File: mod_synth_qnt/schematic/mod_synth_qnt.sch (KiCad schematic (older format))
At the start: 22 parts

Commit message: Update schematic and code
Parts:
- added D? (x3): 1N4148, Diode_THT:D_DO-35_SOD27_P7.62mm_Horizontal, symbol Diode:1N4148
- added J?: Gate, symbol Connector:AudioJack2
- added R? (x3): 10k, symbol Device:R
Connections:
- net GND: now also J?.S, R?.1, R?.1, R?.2
- net IN_1: now also D?.1 (K); no longer C?.1, J?.T
- net IN_2: now also D?.1 (K); no longer C?.1, J?.T
- new net: C?.1, D?.2 (A), J?.T, R?.2 (x2)
- new net: D?.2 (A), J?.T, R?.1
- new net IN_GATE: D?.1 (K)
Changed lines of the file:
@@
 	-1   0    0    -1
 $EndComp
-Text Label 3200 2300 0    50   ~ 0
+Text Label 4300 2300 0    50   ~ 0
 IN_1
-Text Label 3200 3100 0    50   ~ 0
+Text Label 4300 3100 0    50   ~ 0
 IN_2
 $Comp
@@
 Wire Wire Line
 	3200 2950 3200 3000
-Wire Wire Line
-	3200 3100 3075 3100
-Wire Wire Line
-	3200 2300 3075 2300
 Text Label 6225 2925 0    50   ~ 0
 IN_1
@@
 L power:GND #PWR?
 U 1 1 5D619ACB
-P 3075 2600
-F 0 "#PWR?" H 3075 2350 50  0001 C CNN
-F 1 "GND" H 3080 2427 50  0000 C CNN
-F 2 "" H 3075 2600 50  0001 C CNN
-F 3 "" H 3075 2600 50  0001 C CNN
-	1    3075 2600
+P 3075 2675
+F 0 "#PWR?" H 3075 2425 50  0001 C CNN
+F 1 "GND" H 3080 2502 50  0000 C CNN
+F 2 "" H 3075 2675 50  0001 C CNN
+F 3 "" H 3075 2675 50  0001 C CNN
+	1    3075 2675
 	1    0    0    -1
 $EndComp
@@
 L power:GND #PWR?
 U 1 1 5D61A0C8
-P 3075 3375
-F 0 "#PWR?" H 3075 3125 50  0001 C CNN
-F 1 "GND" H 3080 3202 50  0000 C CNN
-F 2 "" H 3075 3375 50  0001 C CNN
-F 3 "" H 3075 3375 50  0001 C CNN
-	1    3075 3375
+P 3075 3450
+F 0 "#PWR?" H 3075 3200 50  0001 C CNN
+F 1 "GND" H 3080 3277 50  0000 C CNN
+F 2 "" H 3075 3450 50  0001 C CNN
+F 3 "" H 3075 3450 50  0001 C CNN
+	1    3075 3450
 	1    0    0    -1
 $EndComp
 Wire Wire Line
 	3075 2600 3075 2500
-Wire Wire Line
-	3075 3300 3075 3375
 $Comp
 L power:GND #PWR?
@@
 NoConn ~ 8275 5300
 NoConn ~ 8275 5200
+$Comp
+L Device:R R?
+U 1 1 5D61316C
+P 3550 2450
+F 0 "R?" V 3343 2450 50  0000 C CNN
+F 1 "10k" V 3434 2450 50  0000 C CNN
+F 2 "" V 3480 2450 50  0001 C CNN
+F 3 "~" H 3550 2450 50  0001 C CNN
+	1    3550 2450
+	-1   0    0    1
+$EndComp
+$Comp
+L Device:R R?
+U 1 1 5D6143B5
+P 3550 3250
+F 0 "R?" V 3343 3250 50  0000 C CNN
+F 1 "10k" V 3434 3250 50  0000 C CNN
+F 2 "" V 3480 3250 50  0001 C CNN
+F 3 "~" H 3550 3250 50  0001 C CNN
+	1    3550 3250
+	-1   0    0    1
+$EndComp
+Wire Wire Line
+	3075 2300 3550 2300
+Wire Wire Line
+	3550 2300 3800 2300
+Connection ~ 3550 2300
+Wire Wire Line
+	3075 3100 3550 3100
+Connection ~ 3550 3100
+Wire Wire Line
+	3550 3100 3800 3100
+Wire Wire Line
+	3550 2600 3075 2600
+Wire Wire Line
+	3075 2600 3075 2675
+Connection ~ 3075 2600
+Wire Wire Line
+	3550 3400 3075 3400
+Wire Wire Line
+	3075 3300 3075 3400
+Connection ~ 3075 3400
+Wire Wire Line
+	3075 3400 3075 3450
+$Comp
+L Connector:AudioJack2 J?
+U 1 1 5D62A188
+P 2800 1650
+F 0 "J?" H 2832 1975 50  0000 C CNN
+F 1 "Gate" H 2832 1884 50  0000 C CNN
+F 2 "" H 2800 1650 50  0001 C CNN
+F 3 "~" H 2800 1650 50  0001 C CNN
+	1    2800 1650
+	1    0    0    -1
+$EndComp
+$Comp
+L power:GND #PWR?
+U 1 1 5D62A425
+P 3200 1225
+F 0 "#PWR?" H 3200 975 50  0001 C CNN
+F 1 "GND" H 3205 1052 50  0000 C CNN
+F 2 "" H 3200 1225 50  0001 C CNN
+F 3 "" H 3200 1225 50  0001 C CNN
+	1    3200 1225
+	-1   0    0    1
+$EndComp
+Wire Wire Line
+	3000 1550 3200 1550
+Text Label 4300 1650 0    50   ~ 0
+IN_GATE
+Wire Wire Line
+	3000 1650 3550 1650
+$Comp
+L Diode:1N4148 D?
+U 1 1 5D630B6B
+P 3925 1650
+F 0 "D?" H 3925 1434 50  0000 C CNN
+F 1 "1N4148" H 3925 1525 50  0000 C CNN
+F 2 "Diode_THT:D_DO-35_SOD27_P7.62mm_Horizontal" H 3925 1475 50  0001 C CNN
+F 3 "https://assets.nexperia.com/documents/data-sheet/1N4148_1N4448.pdf" H 3925 1650 50  0001 C CNN
+	1    3925 1650
+	-1   0    0    1
+$EndComp
+$Comp
+L Diode:1N4148 D?
+U 1 1 5D631B5D
+P 3950 2300
+F 0 "D?" H 3950 2084 50  0000 C CNN
+F 1 "1N4148" H 3950 2175 50  0000 C CNN
+F 2 "Diode_THT:D_DO-35_SOD27_P7.62mm_Horizontal" H 3950 2125 50  0001 C CNN
+F 3 "https://assets.nexperia.com/documents/data-sheet/1N4148_1N4448.pdf" H 3950 2300 50  0001 C CNN
+	1    3950 2300
+	-1   0    0    1
+$EndComp
+$Comp
+L Diode:1N4148 D?
+U 1 1 5D631FDA
+P 3950 3100
+F 0 "D?" H 3950 2884 50  0000 C CNN
+F 1 "1N4148" H 3950 2975 50  0000 C CNN
+F 2 "Diode_THT:D_DO-35_SOD27_P7.62mm_Horizontal" H 3950 2925 50  0001 C CNN
+F 3 "https://assets.nexperia.com/documents/data-sheet/1N4148_1N4448.pdf" H 3950 3100 50  0001 C CNN
+	1    3950 3100
+	-1   0    0    1
+$EndComp
+$Comp
+L Device:R R?
+U 1 1 5D633789
+P 3550 1500
+F 0 "R?" V 3343 1500 50  0000 C CNN
+F 1 "10k" V 3434 1500 50  0000 C CNN
+F 2 "" V 3480 1500 50  0001 C CNN
+F 3 "~" H 3550 1500 50  0001 C CNN
+	1    3550 1500
+	-1   0    0    1
+$EndComp
+Connection ~ 3550 1650
+Wire Wire Line
+	3550 1650 3775 1650
+Wire Wire Line
+	4075 1650 4300 1650
+Wire Wire Line
+	4300 2300 4100 2300
+Wire Wire Line
+	4100 3100 4300 3100
+Wire Wire Line
+	3200 1225 3200 1350
+Wire Wire Line
+	3550 1350 3200 1350
+Connection ~ 3200 1350
+Wire Wire Line
+	3200 1350 3200 1550
 $EndSCHEMATC

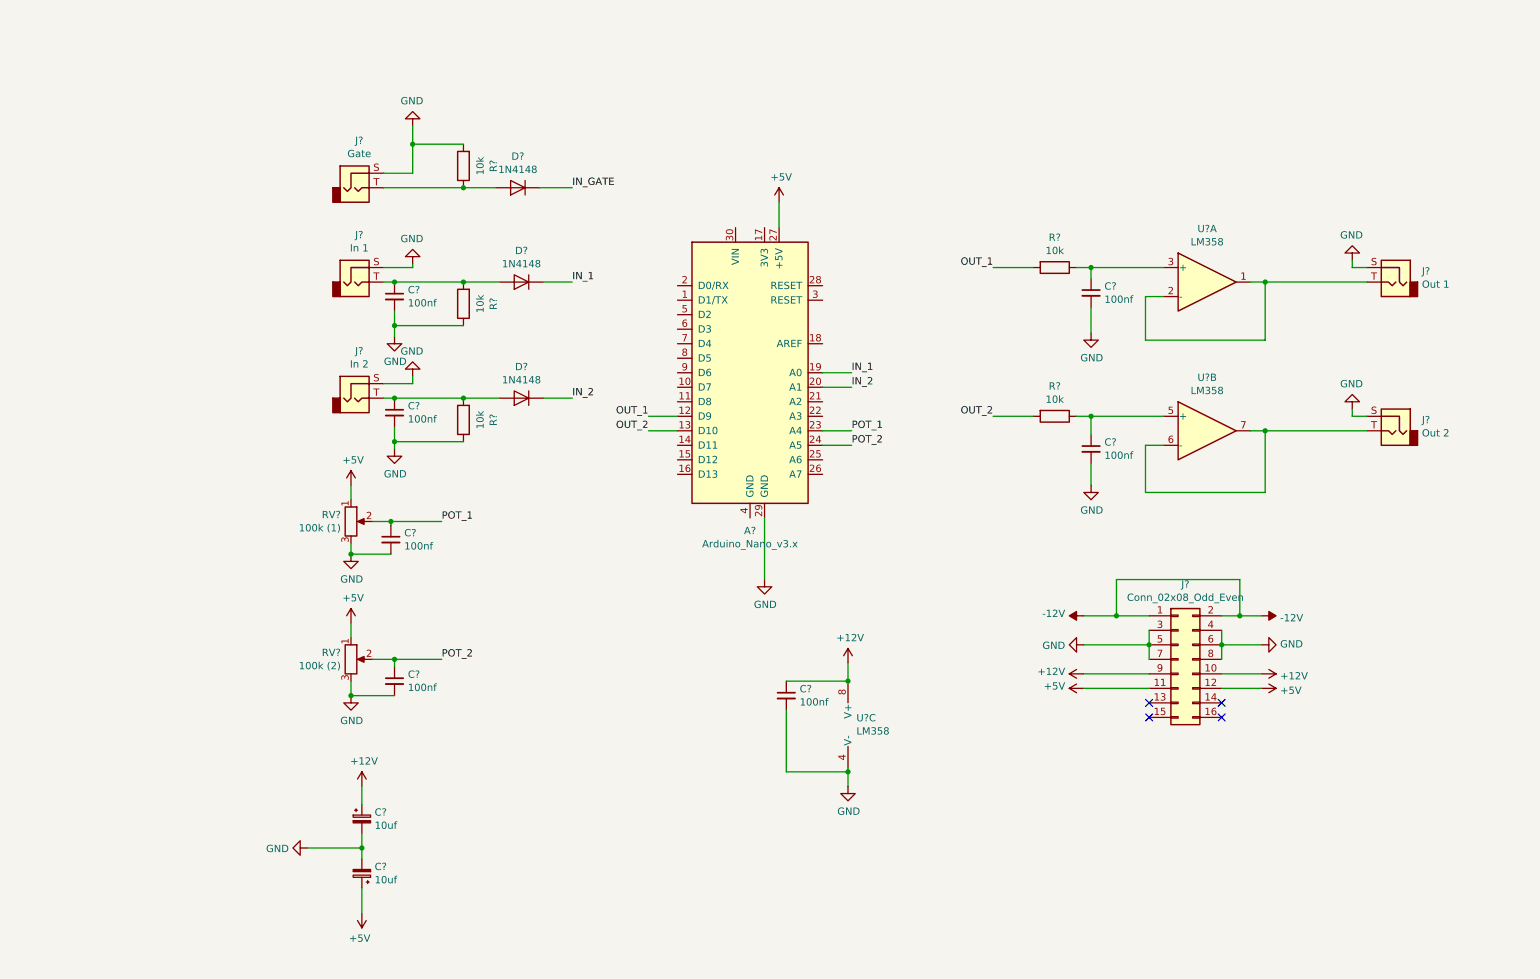
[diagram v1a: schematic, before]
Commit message: Add scale/note input and led output
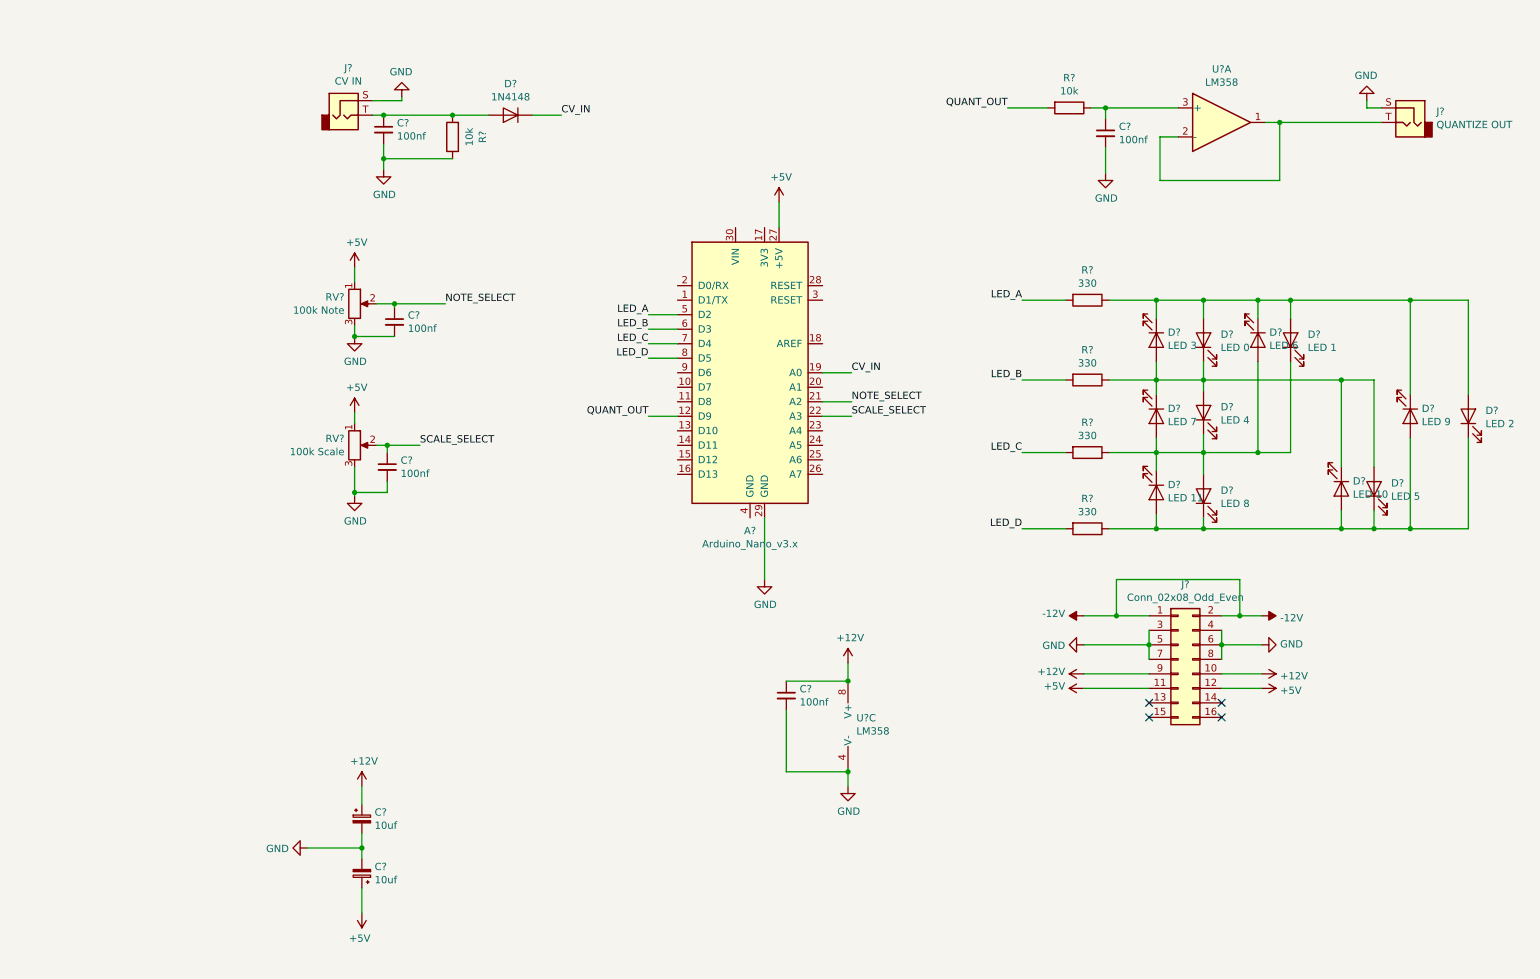
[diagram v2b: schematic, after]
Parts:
- removed C? (x3): 100nf, symbol Device:C_Small
- removed D? (x2): 1N4148, Diode_THT:D_DO-35_SOD27_P7.62mm_Horizontal, symbol Diode:1N4148
- removed J?: Out 2, symbol Connector:AudioJack2
- removed J?: In 2, symbol Connector:AudioJack2
- removed J?: Gate, symbol Connector:AudioJack2
- removed R? (x3): 10k, symbol Device:R
- removed RV?: 100k (2), symbol Device:R_POT
- removed U?: LM358, symbol Amplifier_Operational:LM358
- added C?: 100nf, symbol Device:C_Small
- added D?: LED 3, symbol Device:LED
- added D?: LED 7, symbol Device:LED
- added D?: LED 11, symbol Device:LED
- added D?: LED 6, symbol Device:LED
- added D?: LED 10, symbol Device:LED
- added D?: LED 9, symbol Device:LED
- added D?: LED 2, symbol Device:LED
- added D?: LED 0, symbol Device:LED
- added D?: LED 4, symbol Device:LED
- added D?: LED 8, symbol Device:LED
- added D?: LED 1, symbol Device:LED
- added D?: LED 5, symbol Device:LED
- added R? (x4): 330, symbol Device:R
- added RV?: 100k Scale, symbol Device:R_POT
- J?: value In 1 -> CV IN
- J?: value Out 1 -> QUANTIZE OUT
- RV?: value 100k (1) -> 100k Note
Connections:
- net +5V: now also RV?.1
- net GND: now also C?.2, RV?.3
- net NOTE_SELECT: now reaches A?.21 (A2)
- net NOTE_SELECT: now also C?.1, RV?.2
- net SCALE_SELECT: now reaches A?.22 (A3)
- net SCALE_SELECT: now also C?.1, RV?.2
- net LED_A: now reaches A?.5 (D2)
- net LED_A: now also R?.2
- net LED_B: now reaches A?.6 (D3)
- net LED_B: now also R?.2
- net LED_C: now reaches A?.7 (D4)
- net LED_C: now also R?.2
- net LED_D: now reaches A?.8 (D5)
- net LED_D: now also R?.2
- net IN_1 renamed CV_IN
- net IN_2: no longer names the net of A?.20 (A1)
- net OUT_1 renamed QUANT_OUT
- net OUT_2: no longer names the net of A?.13 (D10)
- removed net POT_1: A?.23 (A4), C?.1, RV?.2
- net POT_2: no longer names the net of A?.24 (A5)
- new net: D?.1 (K), D?.1 (K), D?.1 (K), D?.2 (A), D?.2 (A), D?.2 (A), R?.1 (x4)
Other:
- moved on the sheet: C?, D?, J?, R?, RV?, U?A

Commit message: Improve code, start PCB layout
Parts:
- added J4, J7: Conn_01x07_Male, Connector_PinHeader_2.54mm:PinHeader_1x07_P2.54mm_Vertical, symbol Connector:Conn_01x07_Male
- added J5, J6: Conn_01x07_Female, Connector_PinSocket_2.54mm:PinSocket_1x07_P2.54mm_Vertical, symbol Connector:Conn_01x07_Female
- C1, C2: renamed from C?; footprint (none) -> Capacitor_THT:CP_Radial_D5.0mm_P2.00mm
- C3, C4, C5, C6, C7: renamed from C?; footprint (none) -> Capacitor_THT:C_Disc_D9.0mm_W2.5mm_P5.00mm
- D10, D11, D12, D13, D2, D3, D4, D5, D6, D7, D8, D9: renamed from D?; footprint (none) -> LED_THT:LED_D5.0mm
- J1, J3: renamed from J?; footprint (none) -> Connector_Audio:Jack_3.5mm_QingPu_WQP-PJ398SM_Vertical_CircularHoles
- J2: renamed from J?; footprint (none) -> Connector_IDC:IDC-Header_2x08_P2.54mm_Vertical
- R1, R2, R3, R4, R5, R6: renamed from R?; footprint (none) -> Resistor_THT:R_Axial_DIN0207_L6.3mm_D2.5mm_P10.16mm_Horizontal
- RV1, RV2: renamed from RV?; footprint (none) -> Potentiometer_THT:Potentiometer_Alpha_RD901F-40-00D_Single_Vertical
- U1: renamed from U?; footprint (none) -> Package_DIP:DIP-8_W7.62mm_Socket_LongPads
- gave numbers to parts that had none: 3
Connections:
- net GND: now also J5.1 (Pin_1); no longer C3.2, C4.2, C5.2, J1.S, J3.S, RV1.3, RV2.3
- net CV_IN_PCB_A: now reaches D1.2 (A), R1.2
- net CV_IN_PCB_A: now also J5.6 (Pin_6); no longer C3.1, J1.T
- net Q_OUT_PCB_A: now reaches U1.1, U1.2 (-)
- net Q_OUT_PCB_A: now also J5.7 (Pin_7); no longer J3.T
- new net CV_IN_PCB_B: C3.1, J1.T, J4.6 (Pin_6)
- new net GND_PCB_B: C3.2, C4.2, C5.2, J1.S, J3.S, J4.1 (Pin_1), RV1.3, RV2.3
- new net Q_OUT_PCB_B: J3.T, J4.7 (Pin_7)
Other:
- moved on the sheet: A1, C1, C2, C3, C4, C5, C6, D1, J1, J2, R1, RV1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

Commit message: finish layout
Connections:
- net +5V: now also J5.5 (Pin_5); no longer RV1.1, RV2.1
- net LED_A: now also J6.2 (Pin_2), R3.1; no longer A1.5 (D2), R3.2
- net LED_B: now also J6.3 (Pin_3), R4.1; no longer A1.6 (D3), R4.2
- net LED_C: now also J6.4 (Pin_4), R5.1; no longer A1.7 (D4), R5.2
- net LED_D: now also J6.5 (Pin_5), R6.1; no longer A1.8 (D5), R6.2
- net NOTE_SELECT: now also J6.7 (Pin_7); no longer C5.1, RV1.2
- net SCALE_SELECT: now also J6.6 (Pin_6); no longer C4.1, RV2.2
- net LED_A_PCB_B: now reaches D12.1 (K), D13.2 (A), D2.1 (K), D5.2 (A), D8.1 (K), D9.2 (A)
- net LED_A_PCB_B: now also J7.2 (Pin_2); no longer R3.1
- net LED_B_PCB_B: now reaches D10.1 (K), D11.2 (A), D2.2 (A), D3.1 (K), D5.1 (K), D6.2 (A)
- net LED_B_PCB_B: now also J7.3 (Pin_3); no longer R4.1
- net LED_C_PCB_B: now reaches D3.2 (A), D4.1 (K), D6.1 (K), D7.2 (A), D8.2 (A), D9.1 (K)
- net LED_C_PCB_B: now also J7.4 (Pin_4); no longer R5.1
- net LED_D_PCB_B: now reaches D10.2 (A), D11.1 (K), D12.2 (A), D13.1 (K), D4.2 (A), D7.1 (K)
- net LED_D_PCB_B: now also J7.5 (Pin_5); no longer R6.1
- net 5V_PCB_B: now reaches J4.5 (Pin_5)
- net 5V_PCB_B: now also RV1.1, RV2.1
- net SCALE_SELECT_PCB_B: now reaches J7.6 (Pin_6)
- net SCALE_SELECT_PCB_B: now also C4.1, RV2.2
- net NOTE_SELECT_PCB_B: now reaches J7.7 (Pin_7)
- net NOTE_SELECT_PCB_B: now also C5.1, RV1.2
- new net: A1.5 (D2), R3.2
- new net: A1.6 (D3), R4.2
- new net: A1.7 (D4), R5.2
- new net: A1.8 (D5), R6.2
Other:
- moved on the sheet: R3, R4, R5, R6
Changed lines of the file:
@@
 Wire Wire Line
 	1300 2825 1025 2825
-$Comp
-L power:+5V #PWR0116
-U 1 1 5D6276B5
-P 1025 2350
-F 0 "#PWR0116" H 1025 2200 50  0001 C CNN
-F 1 "+5V" H 1040 2523 50  0000 C CNN
-F 2 "" H 1025 2350 50  0001 C CNN
-F 3 "" H 1025 2350 50  0001 C CNN
-	1    1025 2350
-	1    0    0    -1
-$EndComp
 Wire Wire Line
 	1025 2350 1025 2450
 Text Label 1650 2600 0    50   ~ 0
-NOTE_SELECT
+NOTE_SELECT_PCB_B
 Wire Wire Line
 	1650 2600 1300 2600
@@
 Wire Wire Line
 	3125 1000 2925 1000
-Text Label 3950 1700 2    50   ~ 0
+Text Label 3350 1700 2    50   ~ 0
 LED_A
-Text Label 3950 1800 2    50   ~ 0
+Text Label 3350 1800 2    50   ~ 0
 LED_B
-Text Label 3950 1900 2    50   ~ 0
+Text Label 3350 1900 2    50   ~ 0
 LED_C
-Text Label 3950 2000 2    50   ~ 0
+Text Label 3350 2000 2    50   ~ 0
 LED_D
 Wire Wire Line
-	3950 1700 4150 1700
-Wire Wire Line
-	4150 1800 3950 1800
-Wire Wire Line
-	3950 1900 4150 1900
-Wire Wire Line
-	4150 2000 3950 2000
+	3350 1700 3550 1700
+Wire Wire Line
+	3550 1800 3350 1800
+Wire Wire Line
+	3350 1900 3550 1900
+Wire Wire Line
+	3550 2000 3350 2000
 Text Label 5350 2300 0    50   ~ 0
 NOTE_SELECT
@@
 $EndComp
 $Comp
-L power:+5V #PWR0122
-U 1 1 5D643E11
-P 1000 3625
-F 0 "#PWR0122" H 1000 3475 50  0001 C CNN
-F 1 "+5V" H 1015 3798 50  0000 C CNN
-F 2 "" H 1000 3625 50  0001 C CNN
-F 3 "" H 1000 3625 50  0001 C CNN
-	1    1000 3625
-	1    0    0    -1
-$EndComp
-$Comp
 L Device:C_Small C4
 U 1 1 5D644560
@@
 	1225 4175 1000 4175
 Text Label 1450 3850 0    50   ~ 0
-SCALE_SELECT
+SCALE_SELECT_PCB_B
 Wire Wire Line
 	1150 3850 1225 3850
@@
 L Device:R R3
 U 1 1 5D64DAFD
-P 7850 2425
-F 0 "R3" V 7643 2425 50  0000 C CNN
-F 1 "330" V 7734 2425 50  0000 C CNN
-F 2 "Resistor_THT:R_Axial_DIN0207_L6.3mm_D2.5mm_P10.16mm_Horizontal" V 7780 2425 50  0001 C CNN
-F 3 "~" H 7850 2425 50  0001 C CNN
-	1    7850 2425
-	0    1    1    0
+P 3700 1700
+F 0 "R3" V 3493 1700 50  0000 C CNN
+F 1 "330" V 3584 1700 50  0000 C CNN
+F 2 "Resistor_THT:R_Axial_DIN0207_L6.3mm_D2.5mm_P10.16mm_Horizontal" V 3630 1700 50  0001 C CNN
+F 3 "~" H 3700 1700 50  0001 C CNN
+	1    3700 1700
+	0    -1   -1   0
 $EndComp
 $Comp
 L Device:R R4
 U 1 1 5D64E557
-P 7850 2975
-F 0 "R4" V 7643 2975 50  0000 C CNN
-F 1 "330" V 7734 2975 50  0000 C CNN
-F 2 "Resistor_THT:R_Axial_DIN0207_L6.3mm_D2.5mm_P10.16mm_Horizontal" V 7780 2975 50  0001 C CNN
-F 3 "~" H 7850 2975 50  0001 C CNN
-	1    7850 2975
-	0    1    1    0
+P 3700 1800
+F 0 "R4" V 3493 1800 50  0000 C CNN
+F 1 "330" V 3584 1800 50  0000 C CNN
+F 2 "Resistor_THT:R_Axial_DIN0207_L6.3mm_D2.5mm_P10.16mm_Horizontal" V 3630 1800 50  0001 C CNN
+F 3 "~" H 3700 1800 50  0001 C CNN
+	1    3700 1800
+	0    -1   -1   0
 $EndComp
 $Comp
 L Device:R R5
 U 1 1 5D64EA88
-P 7850 3475
-F 0 "R5" V 7643 3475 50  0000 C CNN
-F 1 "330" V 7734 3475 50  0000 C CNN
-F 2 "Resistor_THT:R_Axial_DIN0207_L6.3mm_D2.5mm_P10.16mm_Horizontal" V 7780 3475 50  0001 C CNN
-F 3 "~" H 7850 3475 50  0001 C CNN
-	1    7850 3475
-	0    1    1    0
+P 3700 1900
+F 0 "R5" V 3493 1900 50  0000 C CNN
+F 1 "330" V 3584 1900 50  0000 C CNN
+F 2 "Resistor_THT:R_Axial_DIN0207_L6.3mm_D2.5mm_P10.16mm_Horizontal" V 3630 1900 50  0001 C CNN
+F 3 "~" H 3700 1900 50  0001 C CNN
+	1    3700 1900
+	0    -1   -1   0
 $EndComp
 $Comp
 L Device:R R6
 U 1 1 5D64ED15
-P 7850 4000
-F 0 "R6" V 7643 4000 50  0000 C CNN
-F 1 "330" V 7734 4000 50  0000 C CNN
-F 2 "Resistor_THT:R_Axial_DIN0207_L6.3mm_D2.5mm_P10.16mm_Horizontal" V 7780 4000 50  0001 C CNN
-F 3 "~" H 7850 4000 50  0001 C CNN
-	1    7850 4000
-	0    1    1    0
+P 3700 2000
+F 0 "R6" V 3493 2000 50  0000 C CNN
+F 1 "330" V 3584 2000 50  0000 C CNN
+F 2 "Resistor_THT:R_Axial_DIN0207_L6.3mm_D2.5mm_P10.16mm_Horizontal" V 3630 2000 50  0001 C CNN
+F 3 "~" H 3700 2000 50  0001 C CNN
+	1    3700 2000
+	0    -1   -1   0
 $EndComp
 $Comp
@@
 	0    -1   -1   0
 $EndComp
-Text Label 7400 2425 2    50   ~ 0
-LED_A
-Text Label 7400 2975 2    50   ~ 0
-LED_B
-Text Label 7400 3475 2    50   ~ 0
-LED_C
-Text Label 7400 4000 2    50   ~ 0
-LED_D
-Wire Wire Line
-	7400 2425 7700 2425
-Wire Wire Line
-	7700 2975 7400 2975
-Wire Wire Line
-	7700 3475 7400 3475
-Wire Wire Line
-	7400 4000 7700 4000
+Wire Wire Line
+	4150 1700 3850 1700
+Wire Wire Line
+	3850 1800 4150 1800
+Wire Wire Line
+	3850 1900 4150 1900
+Wire Wire Line
+	4150 2000 3850 2000
 Wire Wire Line
 	8000 4000 8325 4000
@@
 Wire Wire Line
 	8325 3900 8325 4000
-Connection ~ 8325 4000
 Wire Wire Line
 	8325 4000 8650 4000
@@
 Wire Wire Line
 	8325 2550 8325 2425
-Connection ~ 8325 2425
 Wire Wire Line
 	8325 2425 8000 2425
@@
 	1225 1200 1225 1375
 $Comp
-L power:GND #PWR?
+L power:GND #PWR0112
 U 1 1 5D6EB05E
 P 1900 1300
-F 0 "#PWR?" H 1900 1050 50  0001 C CNN
+F 0 "#PWR0112" H 1900 1050 50  0001 C CNN
 F 1 "GND" H 1905 1127 50  0000 C CNN
 F 2 "" H 1900 1300 50  0001 C CNN
@@
 	1225 1000 1625 1000
 Connection ~ 1225 1000
+Text Label 9225 4950 0    50   ~ 0
+5V_PCB_B
+$Comp
+L power:+5V #PWR0113
+U 1 1 5D6F2729
+P 8450 4950
+F 0 "#PWR0113" H 8450 4800 50  0001 C CNN
+F 1 "+5V" V 8465 5078 50  0000 L CNN
+F 2 "" H 8450 4950 50  0001 C CNN
+F 3 "" H 8450 4950 50  0001 C CNN
+	1    8450 4950
+	0    -1   -1   0
+$EndComp
+Wire Wire Line
+	9225 4950 9075 4950
+Wire Wire Line
+	8625 4950 8450 4950
+Text Label 1000 3625 0    50   ~ 0
+5V_PCB_B
+Text Label 1025 2350 0    50   ~ 0
+5V_PCB_B
+Text Label 9225 5775 0    50   ~ 0
+LED_D_PCB_B
+Text Label 8475 5775 2    50   ~ 0
+LED_D
+Wire Wire Line
+	8625 5775 8475 5775
+Wire Wire Line
+	9075 5775 9225 5775
+Text Label 9225 5575 0    50   ~ 0
+LED_B_PCB_B
+Text Label 8000 4000 2    50   ~ 0
+LED_D_PCB_B
+Text Label 9225 5675 0    50   ~ 0
+LED_C_PCB_B
+Text Label 9225 5475 0    50   ~ 0
+LED_A_PCB_B
+Text Label 8000 3475 2    50   ~ 0
+LED_C_PCB_B
+Text Label 8000 2425 2    50   ~ 0
+LED_A_PCB_B
+Text Label 8000 2975 2    50   ~ 0
+LED_B_PCB_B
+Text Label 8475 5675 2    50   ~ 0
+LED_C
+Wire Wire Line
+	8625 5675 8475 5675
+Wire Wire Line
+	9225 5675 9075 5675
+Connection ~ 8325 2425
+Connection ~ 8325 4000
+Text Label 8475 5575 2    50   ~ 0
+LED_B
+Text Label 8475 5475 2    50   ~ 0
+LED_A
+Wire Wire Line
+	8625 5575 8475 5575
+Wire Wire Line
+	8625 5475 8475 5475
+Wire Wire Line
+	9075 5475 9225 5475
+Wire Wire Line
+	9225 5575 9075 5575
+Text Label 8475 5975 2    50   ~ 0
+NOTE_SELECT
+Text Label 8475 5875 2    50   ~ 0
+SCALE_SELECT
+Wire Wire Line
+	8625 5875 8475 5875
+Wire Wire Line
+	8625 5975 8475 5975
+Text Label 9225 5875 0    50   ~ 0
+SCALE_SELECT_PCB_B
+Text Label 9225 5975 0    50   ~ 0
+NOTE_SELECT_PCB_B
+Wire Wire Line
+	9075 5875 9225 5875
+Wire Wire Line
+	9225 5975 9075 5975
 $EndSCHEMATC
